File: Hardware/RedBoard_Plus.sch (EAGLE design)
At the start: 83 parts, among them IC3 LM1117, J1 DNP, J2 ISP, J3 5.5x2.1mm Barrel, J4 QWIIC_RIGHT_ANGLE, J5 USB Female Type C Connector, Q1 20V/4.2A/52mΩ/1.4W, Q2 310mA/60V/1.6Ω, Q3 310mA/60V/1.6Ω, U1 CH340G, U3 3.3V, U4 ATMEGA328P_TQFP, Y1 16MHz, Y2 12MHz

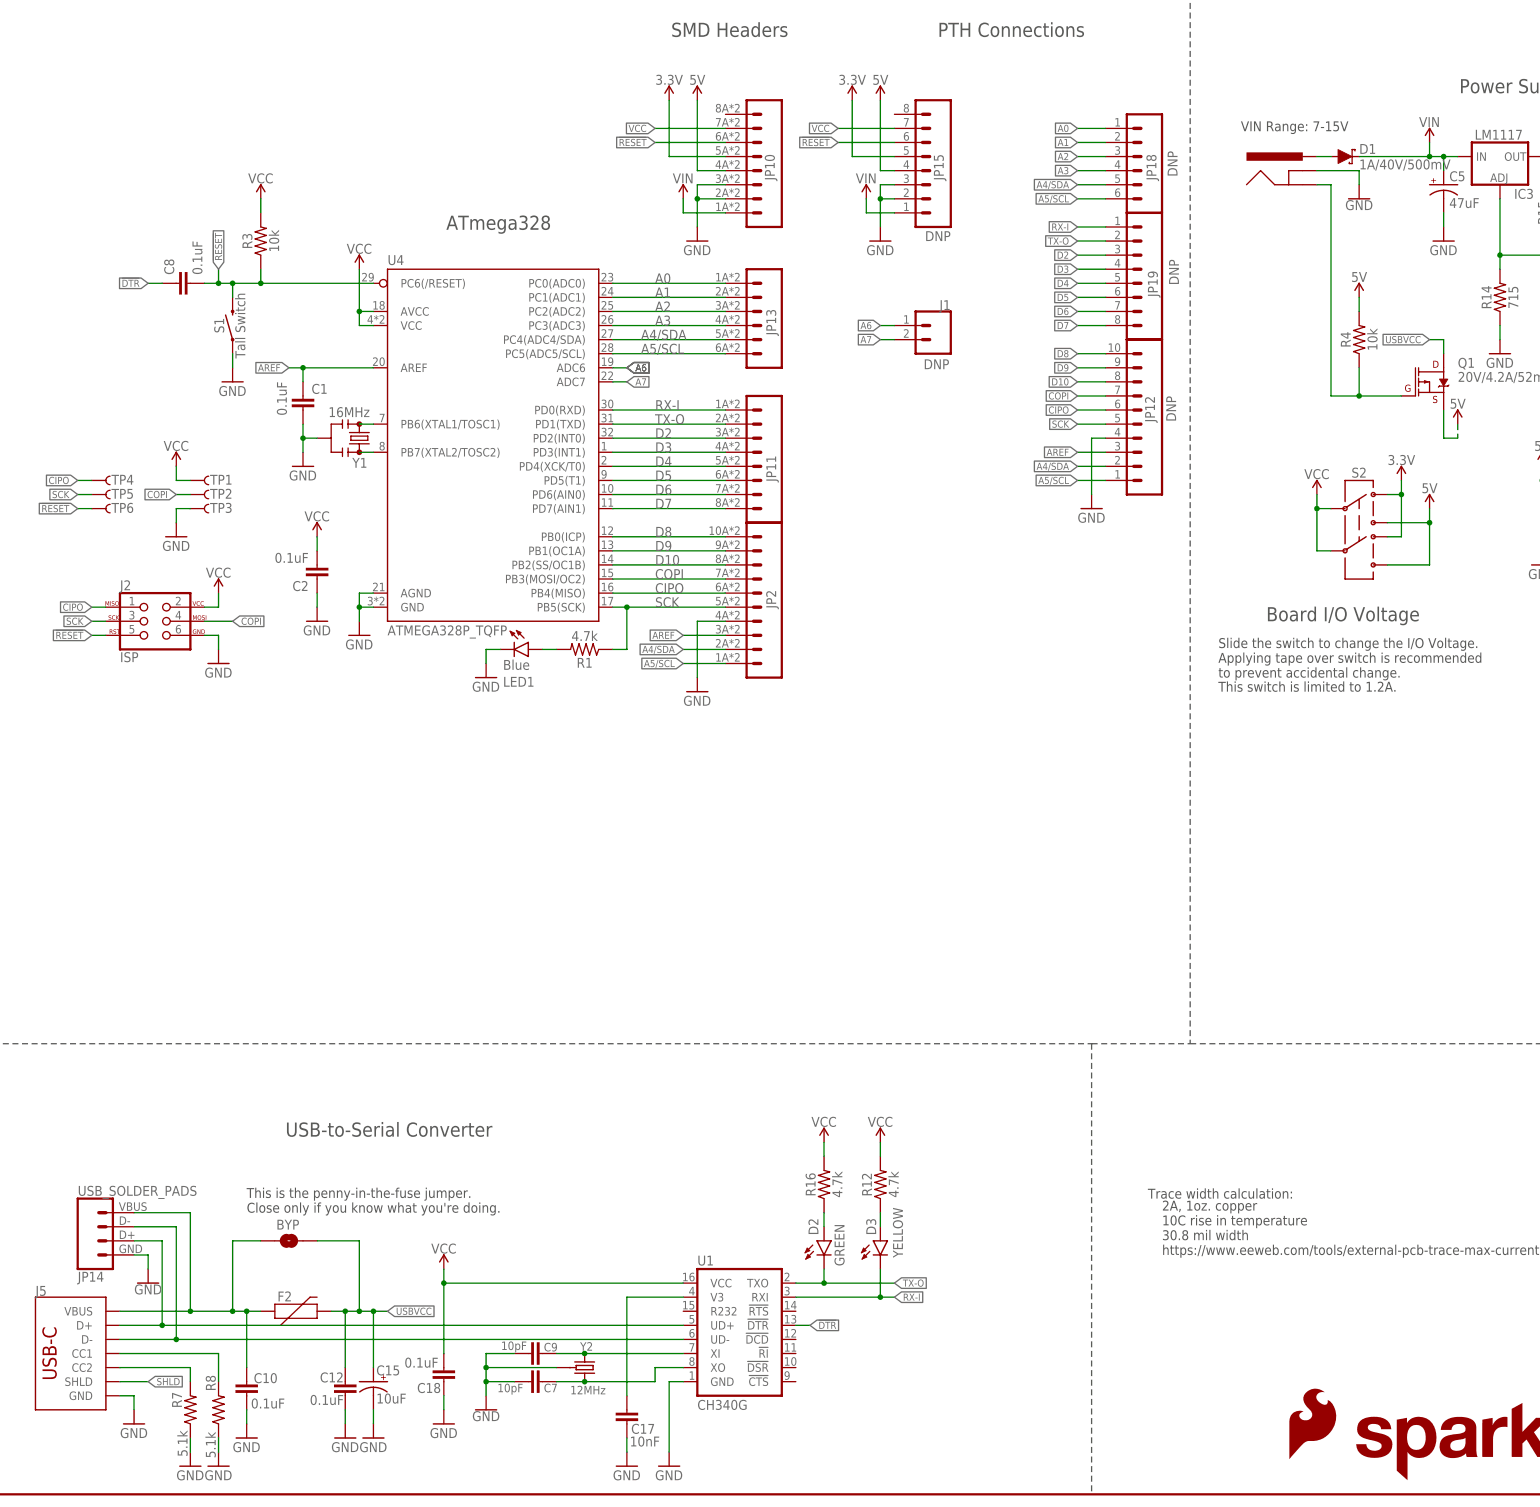
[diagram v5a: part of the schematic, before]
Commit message: Follow Up review changes
Added Qwiic logo device to schematic
Switch RXO/TXI signals at CH340G. Switched the order of LEDs as well
Updated headers to use current library parts
Updated ISP header sch symbol to use COPI/CIPO
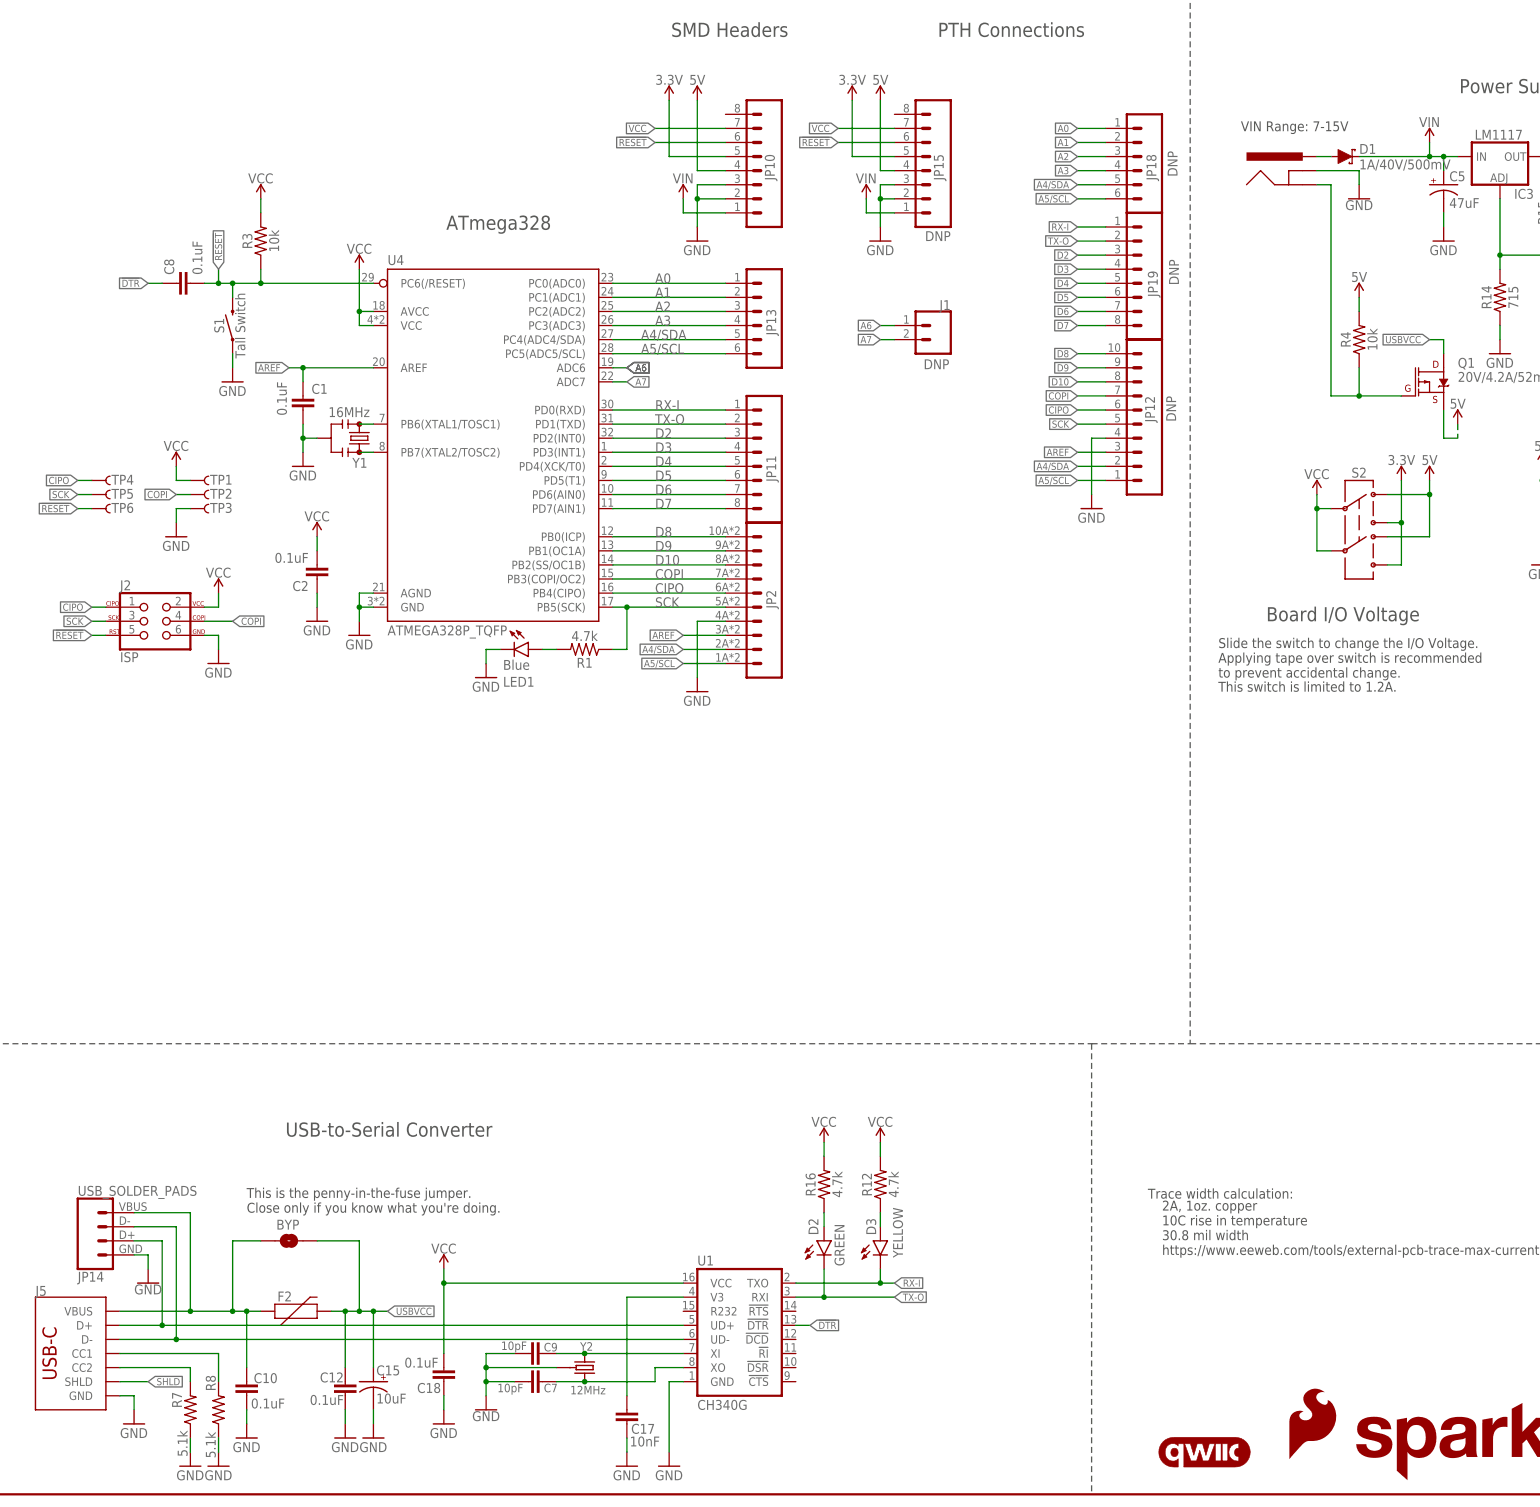
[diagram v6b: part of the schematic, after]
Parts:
- added LOGO1: QWIIC_LOGO_5MM, SparkFun-Aesthetics:QWIIC_LOGO_5MM
- JP10, JP11: device SparkFun-Connectors:M08SMD-COMBO -> SparkFun-Connectors:CONN_08SMD-COMBO-FEMALE
- JP12: device SparkFun-Connectors:M10NO_SILK -> SparkFun-Connectors:CONN_10NO_SILK_PTH_FEMALE
- JP13: device SparkFun-Connectors:M06SMD-STRAIGHT-COMBO -> SparkFun-Connectors:CONN_06SMD-STRAIGHT-COMBO-FEMALE
- JP15: device SparkFun-Connectors:M08NO_SILK -> SparkFun-Connectors:CONN_08NO_SILK_DNP
- JP18: device SparkFun-Connectors:M06NO_SILK -> SparkFun-Connectors:CONN_06NO_SILK_NO_POP
- JP19: device SparkFun-Connectors:CONN_08NO_SILK_FEMALE_PTH -> SparkFun-Connectors:CONN_08NO_SILK_DNP
- JP2: value M10SMD_COMBO -> (none); device SparkFun-Connectors:M10SMD_COMBO -> SparkFun-Connectors:CONN_10SMD_COMBO-FEMALE
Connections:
- net CIPO: now also U4.PB4(CIPO); no longer U4.PB4(MISO)
- net COPI: now also U4.PB3(COPI/OC2); no longer U4.PB3(MOSI/OC2)
- net RX-I: now also U1.TXO; no longer U1.RXI
- net TX-O: now also U1.RXI; no longer U1.TXO
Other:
- moved on the sheet: JP10, JP13

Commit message: Update prod_id on isp header
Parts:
- J2: PROD_ID (none) -> CONN-11415
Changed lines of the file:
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@@
 <grid distance="0.1" unitdist="inch" unit="inch" style="lines" multiple="1" display="no" altdistance="0.01" altunitdist="inch" altunit="inch"/>
 <layers>
-<layer number="1" name="Top" color="4" fill="1" visible="yes" active="no"/>
-<layer number="2" name="Route2" color="1" fill="3" visible="yes" active="no"/>
-<layer number="3" name="Route3" color="4" fill="3" visible="yes" active="no"/>
-<layer number="4" name="Route4" color="1" fill="4" visible="yes" active="no"/>
-<layer number="5" name="Route5" color="4" fill="4" visible="yes" active="no"/>
-<layer number="6" name="Route6" color="1" fill="8" visible="yes" active="no"/>
-<layer number="7" name="Route7" color="4" fill="8" visible="yes" active="no"/>
-<layer number="8" name="Route8" color="1" fill="2" visible="yes" active="no"/>
-<layer number="9" name="Route9" color="4" fill="2" visible="yes" active="no"/>
-<layer number="10" name="Route10" color="1" fill="7" visible="yes" active="no"/>
-<layer number="11" name="Route11" color="4" fill="7" visible="yes" active="no"/>
-<layer number="12" name="Route12" color="1" fill="5" visible="yes" active="no"/>
-<layer number="13" name="Route13" color="4" fill="5" visible="yes" active="no"/>
-<layer number="14" name="Route14" color="1" fill="6" visible="yes" active="no"/>
-<layer number="15" name="Route15" color="4" fill="6" visible="yes" active="no"/>
-<layer number="16" name="Bottom" color="1" fill="1" visible="yes" active="no"/>
-<layer number="17" name="Pads" color="2" fill="1" visible="yes" active="no"/>
-<layer number="18" name="Vias" color="2" fill="1" visible="yes" active="no"/>
-<layer number="19" name="Unrouted" color="6" fill="1" visible="yes" active="no"/>
-<layer number="20" name="Dimension" color="24" fill="1" visible="yes" active="no"/>
-<layer number="21" name="tPlace" color="16" fill="1" visible="yes" active="no"/>
-<layer number="22" name="bPlace" color="14" fill="1" visible="yes" active="no"/>
-<layer number="23" name="tOrigins" color="15" fill="1" visible="yes" active="no"/>
-<layer number="24" name="bOrigins" color="15" fill="1" visible="yes" active="no"/>
-<layer number="25" name="tNames" color="7" fill="1" visible="yes" active="no"/>
-<layer number="26" name="bNames" color="7" fill="1" visible="yes" active="no"/>
-<layer number="27" name="tValues" color="7" fill="1" visible="yes" active="no"/>
-<layer number="28" name="bValues" color="7" fill="1" visible="yes" active="no"/>
+<layer number="1" name="Top" color="4" fill="1" visible="no" active="no"/>
+<layer number="2" name="Route2" color="1" fill="3" visible="no" active="no"/>
+<layer number="3" name="Route3" color="4" fill="3" visible="no" active="no"/>
+<layer number="4" name="Route4" color="1" fill="4" visible="no" active="no"/>
+<layer number="5" name="Route5" color="4" fill="4" visible="no" active="no"/>
+<layer number="6" name="Route6" color="1" fill="8" visible="no" active="no"/>
+<layer number="7" name="Route7" color="4" fill="8" visible="no" active="no"/>
+<layer number="8" name="Route8" color="1" fill="2" visible="no" active="no"/>
+<layer number="9" name="Route9" color="4" fill="2" visible="no" active="no"/>
+<layer number="10" name="Route10" color="1" fill="7" visible="no" active="no"/>
+<layer number="11" name="Route11" color="4" fill="7" visible="no" active="no"/>
+<layer number="12" name="Route12" color="1" fill="5" visible="no" active="no"/>
+<layer number="13" name="Route13" color="4" fill="5" visible="no" active="no"/>
+<layer number="14" name="Route14" color="1" fill="6" visible="no" active="no"/>
+<layer number="15" name="Route15" color="4" fill="6" visible="no" active="no"/>
+<layer number="16" name="Bottom" color="1" fill="1" visible="no" active="no"/>
+<layer number="17" name="Pads" color="2" fill="1" visible="no" active="no"/>
+<layer number="18" name="Vias" color="2" fill="1" visible="no" active="no"/>
+<layer number="19" name="Unrouted" color="6" fill="1" visible="no" active="no"/>
+<layer number="20" name="Dimension" color="24" fill="1" visible="no" active="no"/>
+<layer number="21" name="tPlace" color="16" fill="1" visible="no" active="no"/>
+<layer number="22" name="bPlace" color="14" fill="1" visible="no" active="no"/>
+<layer number="23" name="tOrigins" color="15" fill="1" visible="no" active="no"/>
+<layer number="24" name="bOrigins" color="15" fill="1" visible="no" active="no"/>
+<layer number="25" name="tNames" color="7" fill="1" visible="no" active="no"/>
+<layer number="26" name="bNames" color="7" fill="1" visible="no" active="no"/>
+<layer number="27" name="tValues" color="7" fill="1" visible="no" active="no"/>
+<layer number="28" name="bValues" color="7" fill="1" visible="no" active="no"/>
 <layer number="29" name="tStop" color="2" fill="3" visible="no" active="no"/>
 <layer number="30" name="bStop" color="5" fill="6" visible="no" active="no"/>
@@
 <layer number="35" name="tGlue" color="7" fill="4" visible="no" active="no"/>
 <layer number="36" name="bGlue" color="7" fill="5" visible="no" active="no"/>
-<layer number="37" name="tTest" color="7" fill="1" visible="yes" active="no"/>
-<layer number="38" name="bTest" color="7" fill="1" visible="yes" active="no"/>
+<layer number="37" name="tTest" color="7" fill="1" visible="no" active="no"/>
+<layer number="38" name="bTest" color="7" fill="1" visible="no" active="no"/>
 <layer number="39" name="tKeepout" color="4" fill="11" visible="no" active="no"/>
 <layer number="40" name="bKeepout" color="1" fill="11" visible="no" active="no"/>
@@
 <layer number="44" name="Drills" color="7" fill="1" visible="no" active="no"/>
 <layer number="45" name="Holes" color="7" fill="1" visible="no" active="no"/>
-<layer number="46" name="Milling" color="3" fill="1" visible="yes" active="no"/>
-<layer number="47" name="Measures" color="7" fill="1" visible="yes" active="no"/>
-<layer number="48" name="Document" color="7" fill="1" visible="yes" active="no"/>
-<layer number="49" name="Reference" color="13" fill="1" visible="yes" active="no"/>
-<layer number="50" name="dxf" color="12" fill="1" visible="yes" active="no"/>
-<layer number="51" name="tDocu" color="6" fill="1" visible="yes" active="no"/>
-<layer number="52" name="bDocu" color="7" fill="1" visible="yes" active="no"/>
-<layer number="53" name="tGND_GNDA" color="7" fill="1" visible="yes" active="no"/>
-<layer number="54" name="bGND_GNDA" color="7" fill="1" visible="yes" active="no"/>
-<layer number="56" name="wert" color="7" fill="1" visible="yes" active="no"/>
-<layer number="57" name="tCAD" color="7" fill="1" visible="yes" active="no"/>
-<layer number="59" name="tCarbon" color="7" fill="1" visible="yes" active="no"/>
-<layer number="60" name="bCarbon" color="7" fill="1" visible="yes" active="no"/>
+<layer number="46" name="Milling" color="3" fill="1" visible="no" active="no"/>
+<layer number="47" name="Measures" color="7" fill="1" visible="no" active="no"/>
+<layer number="48" name="Document" color="7" fill="1" visible="no" active="no"/>
+<layer number="49" name="Reference" color="13" fill="1" visible="no" active="no"/>
+<layer number="50" name="dxf" color="12" fill="1" visible="no" active="no"/>
+<layer number="51" name="tDocu" color="6" fill="1" visible="no" active="no"/>
+<layer number="52" name="bDocu" color="7" fill="1" visible="no" active="no"/>
+<layer number="53" name="tGND_GNDA" color="7" fill="1" visible="no" active="no"/>
+<layer number="54" name="bGND_GNDA" color="7" fill="1" visible="no" active="no"/>
+<layer number="56" name="wert" color="7" fill="1" visible="no" active="no"/>
+<layer number="57" name="tCAD" color="7" fill="1" visible="no" active="no"/>
+<layer number="59" name="tCarbon" color="7" fill="1" visible="no" active="no"/>
+<layer number="60" name="bCarbon" color="7" fill="1" visible="no" active="no"/>
 <layer number="88" name="SimResults" color="9" fill="1" visible="yes" active="yes"/>
 <layer number="89" name="SimProbes" color="9" fill="1" visible="yes" active="yes"/>
@@
 <part name="JP1" library="SparkFun-Aesthetics" deviceset="SFE_LOGO_NAME" device=".1_INCH"/>
 <part name="JP7" library="SparkFun-Aesthetics" deviceset="SFE_LOGO_FLAME" device=".1_INCH"/>
-<part name="J2" library="SparkFun-Connectors" deviceset="AVR_SPI_PROG_3X2" device="SMD" value="ISP"/>
+<part name="J2" library="SparkFun-Connectors" deviceset="AVR_SPI_PROG_3X2" device="SMD" value="ISP">
+<attribute name="PROD_ID" value="CONN-11415"/>
+</part>
 <part name="C6" library="SparkFun-Capacitors" deviceset="10UF-POLAR" device="-EIA3216-16V-10%(TANT)" value="10uF"/>
 <part name="GND14" library="SparkFun-PowerSymbols" deviceset="GND" device=""/>
@@
 <attribute name="NAME" x="22.86" y="163.068" size="1.778" layer="95" font="vector"/>
 <attribute name="VALUE" x="22.86" y="150.114" size="1.778" layer="96" font="vector"/>
+<attribute name="PROD_ID" x="27.94" y="157.48" size="1.27" layer="96" display="off"/>
 </instance>
 <instance part="C6" gate="G$1" x="314.96" y="177.8" smashed="yes">
